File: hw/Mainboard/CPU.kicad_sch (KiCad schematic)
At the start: 10 parts, among them U11 W65C02S, U12 AS6C1008

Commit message: wip: pre-routing
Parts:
- removed JP7: A10 SEL, Jumper:SolderJumper-3_P1.3mm_Open_RoundedPad1.0x1.5mm, symbol Jumper:SolderJumper_3_Open
- removed JP8: A11 SEL, Jumper:SolderJumper-3_P1.3mm_Open_RoundedPad1.0x1.5mm, symbol Jumper:SolderJumper_3_Open
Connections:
- net RAM_A10: now also U12.31 (A15)
- net RAM_A11: now also U12.28 (A13)
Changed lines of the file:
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@@
-    (stroke (width 0) (type default) (color 0 0 0 0))
-  )
-  (bus_entry (at 148.59 43.18) (size -2.54 2.54)
     (stroke (width 0) (type default) (color 0 0 0 0))
   )
@@
     (stroke (width 0) (type default) (color 0 0 0 0))
   )
-  (bus_entry (at 148.59 36.83) (size -2.54 2.54)
-    (stroke (width 0) (type default) (color 0 0 0 0))
-  )
   (bus_entry (at 218.44 67.31) (size 2.54 -2.54)
     (stroke (width 0) (type default) (color 0 0 0 0))
@@
     (stroke (width 0) (type default) (color 0 0 0 0))
   )
-  (wire (pts (xy 167.64 36.83) (xy 218.44 36.83))
+  (wire (pts (xy 162.56 36.83) (xy 218.44 36.83))
     (stroke (width 0) (type default) (color 0 0 0 0))
   )
@@
     (stroke (width 0) (type default) (color 0 0 0 0))
   )
-  (wire (pts (xy 148.59 43.18) (xy 167.64 43.18))
-    (stroke (width 0) (type default) (color 0 0 0 0))
-  )
   (wire (pts (xy 162.56 95.25) (xy 185.42 95.25))
     (stroke (width 0) (type default) (color 0 0 0 0))
@@
     (stroke (width 0) (type default) (color 0 0 0 0))
   )
-  (wire (pts (xy 172.72 46.99) (xy 172.72 90.17))
+  (wire (pts (xy 172.72 43.18) (xy 172.72 90.17))
     (stroke (width 0) (type default) (color 0 0 0 0))
   )
@@
     (stroke (width 0) (type default) (color 0 0 0 0))
   )
-  (bus (pts (xy 146.05 39.37) (xy 146.05 29.21))
-    (stroke (width 0) (type default) (color 0 0 0 0))
-  )
   (bus (pts (xy 124.46 95.25) (xy 124.46 97.79))
     (stroke (width 0) (type default) (color 0 0 0 0))
@@
     (stroke (width 0) (type default) (color 0 0 0 0))
   )
-  (bus (pts (xy 146.05 59.69) (xy 146.05 45.72))
-    (stroke (width 0) (type default) (color 0 0 0 0))
-  )
   (wire (pts (xy 148.59 69.85) (xy 185.42 69.85))
     (stroke (width 0) (type default) (color 0 0 0 0))
@@
     (stroke (width 0) (type default) (color 0 0 0 0))
   )
-  (wire (pts (xy 162.56 95.25) (xy 162.56 40.64))
+  (wire (pts (xy 162.56 36.83) (xy 162.56 95.25))
     (stroke (width 0) (type default) (color 0 0 0 0))
   )
@@
     (stroke (width 0) (type default) (color 0 0 0 0))
   )
-  (bus (pts (xy 146.05 45.72) (xy 146.05 39.37))
+  (bus (pts (xy 146.05 29.21) (xy 146.05 59.69))
     (stroke (width 0) (type default) (color 0 0 0 0))
   )
@@
     (stroke (width 0) (type default) (color 0 0 0 0))
   )
-  (wire (pts (xy 148.59 36.83) (xy 157.48 36.83))
-    (stroke (width 0) (type default) (color 0 0 0 0))
-  )
   (wire (pts (xy 73.66 80.01) (xy 87.63 80.01))
     (stroke (width 0) (type default) (color 0 0 0 0))
@@
     (stroke (width 0) (type default) (color 0 0 0 0))
   )
-  (wire (pts (xy 177.8 43.18) (xy 218.44 43.18))
+  (wire (pts (xy 172.72 43.18) (xy 218.44 43.18))
     (stroke (width 0) (type default) (color 0 0 0 0))
   )
@@
     (effects (font (size 1.27 1.27)) (justify left bottom))
   )
-  (label "A10" (at 148.59 36.83 0)
-    (effects (font (size 1.27 1.27)) (justify left bottom))
-  )
   (label "D5" (at 118.11 113.03 0)
     (effects (font (size 1.27 1.27)) (justify left bottom))
@@
   (label "D6" (at 218.44 59.69 180)
     (effects (font (size 1.27 1.27)) (justify right bottom))
-  )
-  (label "A11" (at 148.59 43.18 0)
-    (effects (font (size 1.27 1.27)) (justify left bottom))
   )
   (label "A2" (at 148.59 87.63 0)
@@
     (pin "2")
   )
-  (symbol (lib_id "Jumper:SolderJumper_3_Open") (at 162.56 36.83 0) (mirror y) (unit 1)
-    (in_bom yes) (on_board yes)
-    (property "Reference" "JP7" (id 0) (at 162.56 31.75 0))
-    (property "Value" "A10 SEL" (id 1) (at 162.56 34.29 0))
-    (property "Footprint" "Jumper:SolderJumper-3_P1.3mm_Open_RoundedPad1.0x1.5mm" (id 2) (at 162.56 36.83 0)
-      (effects (font (size 1.27 1.27)) hide)
-    )
-    (property "Datasheet" "~" (id 3) (at 162.56 36.83 0)
-      (effects (font (size 1.27 1.27)) hide)
-    )
-    (pin "1")
-    (pin "2")
-    (pin "3")
-  )
-  (symbol (lib_id "Jumper:SolderJumper_3_Open") (at 172.72 43.18 0) (mirror y) (unit 1)
-    (in_bom yes) (on_board yes)
-    (property "Reference" "JP8" (id 0) (at 172.72 38.1 0))
-    (property "Value" "A11 SEL" (id 1) (at 172.72 40.64 0))
-    (property "Footprint" "Jumper:SolderJumper-3_P1.3mm_Open_RoundedPad1.0x1.5mm" (id 2) (at 172.72 43.18 0)
-      (effects (font (size 1.27 1.27)) hide)
-    )
-    (property "Datasheet" "~" (id 3) (at 172.72 43.18 0)
-      (effects (font (size 1.27 1.27)) hide)
-    )
-    (pin "1")
-    (pin "2")
-    (pin "3")
-  )
   (symbol (lib_id "power:GND") (at 102.87 124.46 0) (unit 1)

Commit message: Document schematics
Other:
- note added: "To improve routing, A[0..16] and D[0..7] and arbitrarily assigned to the address and data pins of the SRAM. RAM_A[10..11] are used to mirror the screen RAM when the CPU accesses range $8000-8FFF. 40 col PET has 1k of screen RAM, mirrored 4 times. 80 col PET has 2k of screen RAM, mirrored 2 times."
- note removed: "40 col PET has 1k of video RAM, mirrored 4 times. 80 col PET has 2k of video RAM, mirrored 2 times. 111111 addr 5432109876543210 8000: 1000000000000000 8400: 1000010000000000 8800: 1000100000000000 8C00: 1000110000000000"
- note removed: "TODO: Reroute RAM Addr and Data"
- moved on the sheet: C10, C11
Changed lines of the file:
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@@
   (junction (at 68.58 57.15) (diameter 0) (color 0 0 0 0)
   )
-  (junction (at 55.88 156.21) (diameter 0) (color 0 0 0 0)
+  (junction (at 71.12 170.18) (diameter 0) (color 0 0 0 0)
   )
   (junction (at 78.74 77.47) (diameter 0) (color 0 0 0 0)
@@
   (junction (at 68.58 46.99) (diameter 0) (color 0 0 0 0)
   )
-  (junction (at 55.88 148.59) (diameter 0) (color 0 0 0 0)
+  (junction (at 71.12 162.56) (diameter 0) (color 0 0 0 0)
   )
   (no_connect (at 87.63 107.95))
@@
     (stroke (width 0) (type default) (color 0 0 0 0))
   )
-  (wire (pts (xy 55.88 148.59) (xy 66.04 148.59))
+  (wire (pts (xy 71.12 162.56) (xy 81.28 162.56))
     (stroke (width 0) (type default) (color 0 0 0 0))
   )
@@
     (stroke (width 0) (type default) (color 0 0 0 0))
   )
-  (wire (pts (xy 66.04 154.94) (xy 66.04 156.21))
-    (stroke (width 0) (type default) (color 0 0 0 0))
-  )
-  (wire (pts (xy 66.04 156.21) (xy 55.88 156.21))
+  (wire (pts (xy 81.28 168.91) (xy 81.28 170.18))
+    (stroke (width 0) (type default) (color 0 0 0 0))
+  )
+  (wire (pts (xy 81.28 170.18) (xy 71.12 170.18))
     (stroke (width 0) (type default) (color 0 0 0 0))
   )
@@
     (stroke (width 0) (type default) (color 0 0 0 0))
   )
-  (wire (pts (xy 45.72 149.86) (xy 45.72 148.59))
+  (wire (pts (xy 60.96 163.83) (xy 60.96 162.56))
     (stroke (width 0) (type default) (color 0 0 0 0))
   )
@@
     (stroke (width 0) (type default) (color 0 0 0 0))
   )
-  (wire (pts (xy 45.72 156.21) (xy 45.72 154.94))
+  (wire (pts (xy 60.96 170.18) (xy 60.96 168.91))
     (stroke (width 0) (type default) (color 0 0 0 0))
   )
@@
     (stroke (width 0) (type default) (color 0 0 0 0))
   )
-  (wire (pts (xy 55.88 156.21) (xy 45.72 156.21))
+  (wire (pts (xy 71.12 170.18) (xy 60.96 170.18))
     (stroke (width 0) (type default) (color 0 0 0 0))
   )
@@
     (stroke (width 0) (type default) (color 0 0 0 0))
   )
-  (wire (pts (xy 45.72 148.59) (xy 55.88 148.59))
+  (wire (pts (xy 60.96 162.56) (xy 71.12 162.56))
     (stroke (width 0) (type default) (color 0 0 0 0))
   )
@@
     (stroke (width 0) (type default) (color 0 0 0 0))
   )
-  (wire (pts (xy 66.04 148.59) (xy 66.04 149.86))
+  (wire (pts (xy 81.28 162.56) (xy 81.28 163.83))
     (stroke (width 0) (type default) (color 0 0 0 0))
   )
@@
     (stroke (width 0) (type default) (color 0 0 0 0))
   )
-  (text "TODO: Reroute RAM Addr and Data" (at 227.33 104.14 0)
+  (text "To improve routing, A[0..16] and D[0..7] and arbitrarily assigned to\nthe address and data pins of the SRAM.\n\nRAM_A[10..11] are used to mirror the screen RAM when the CPU accesses\nrange $8000-8FFF.\n\n40 col PET has 1k of screen RAM, mirrored 4 times.\n80 col PET has 2k of screen RAM, mirrored 2 times.\n"
+    (at 166.37 148.59 0)
     (effects (font (size 1.27 1.27)) (justify left bottom))
   )
   (text " RAM\n128KB" (at 195.58 86.36 0)
-    (effects (font (size 1.27 1.27)) (justify left bottom))
-  )
-  (text "40 col PET has 1k of video RAM, mirrored 4 times.\n80 col PET has 2k of video RAM, mirrored 2 times.\n\n      111111\naddr  5432109876543210\n8000: 1000000000000000\n8400: 1000010000000000\n8800: 1000100000000000\n8C00: 1000110000000000\n"
-    (at 143.51 160.02 0)
     (effects (font (size 1.27 1.27)) (justify left bottom))
   )
@@
     (pin "2")
   )
-  (symbol (lib_id "Device:C_Small") (at 45.72 152.4 0) (unit 1)
-    (in_bom yes) (on_board yes)
-    (property "Reference" "C10" (id 0) (at 48.0568 151.2316 0)
+  (symbol (lib_id "Device:C_Small") (at 60.96 166.37 0) (unit 1)
+    (in_bom yes) (on_board yes)
+    (property "Reference" "C10" (id 0) (at 63.2968 165.2016 0)
       (effects (font (size 1.27 1.27)) (justify left))
     )
-    (property "Value" "100n" (id 1) (at 48.0568 153.543 0)
+    (property "Value" "100n" (id 1) (at 63.2968 167.513 0)
       (effects (font (size 1.27 1.27)) (justify left))
     )
-    (property "Footprint" "Capacitor_SMD:C_0402_1005Metric" (id 2) (at 45.72 152.4 0)
-      (effects (font (size 1.27 1.27)) hide)
-    )
-    (property "Datasheet" "~" (id 3) (at 45.72 152.4 0)
-      (effects (font (size 1.27 1.27)) hide)
-    )
-    (property "LCSC" "C1525" (id 4) (at 45.72 152.4 0)
+    (property "Footprint" "Capacitor_SMD:C_0402_1005Metric" (id 2) (at 60.96 166.37 0)
+      (effects (font (size 1.27 1.27)) hide)
+    )
+    (property "Datasheet" "~" (id 3) (at 60.96 166.37 0)
+      (effects (font (size 1.27 1.27)) hide)
+    )
+    (property "LCSC" "C1525" (id 4) (at 60.96 166.37 0)
       (effects (font (size 1.27 1.27)) hide)
     )
@@
     (pin "2")
   )
-  (symbol (lib_id "Device:C_Small") (at 66.04 152.4 0) (unit 1)
-    (in_bom yes) (on_board yes)
-    (property "Reference" "C11" (id 0) (at 68.3768 151.2316 0)
+  (symbol (lib_id "Device:C_Small") (at 81.28 166.37 0) (unit 1)
+    (in_bom yes) (on_board yes)
+    (property "Reference" "C11" (id 0) (at 83.6168 165.2016 0)
       (effects (font (size 1.27 1.27)) (justify left))
     )
-    (property "Value" "100n" (id 1) (at 68.3768 153.543 0)
+    (property "Value" "100n" (id 1) (at 83.6168 167.513 0)
       (effects (font (size 1.27 1.27)) (justify left))
     )
-    (property "Footprint" "Capacitor_SMD:C_0402_1005Metric" (id 2) (at 66.04 152.4 0)
-      (effects (font (size 1.27 1.27)) hide)
-    )
-    (property "Datasheet" "~" (id 3) (at 66.04 152.4 0)
-      (effects (font (size 1.27 1.27)) hide)
-    )
-    (property "LCSC" "C1525" (id 4) (at 66.04 152.4 0)
+    (property "Footprint" "Capacitor_SMD:C_0402_1005Metric" (id 2) (at 81.28 166.37 0)
+      (effects (font (size 1.27 1.27)) hide)
+    )
+    (property "Datasheet" "~" (id 3) (at 81.28 166.37 0)
+      (effects (font (size 1.27 1.27)) hide)
+    )
+    (property "LCSC" "C1525" (id 4) (at 81.28 166.37 0)
       (effects (font (size 1.27 1.27)) hide)
     )
@@
     (pin "2")
   )
-  (symbol (lib_id "power:+3V3") (at 55.88 148.59 0) (unit 1)
-    (in_bom yes) (on_board yes)
-    (property "Reference" "#PWR047" (id 0) (at 55.88 152.4 0)
-      (effects (font (size 1.27 1.27)) hide)
-    )
-    (property "Value" "+3V3" (id 1) (at 56.261 144.1958 0))
-    (property "Footprint" "" (id 2) (at 55.88 148.59 0)
-      (effects (font (size 1.27 1.27)) hide)
-    )
-    (property "Datasheet" "" (id 3) (at 55.88 148.59 0)
-      (effects (font (size 1.27 1.27)) hide)
-    )
-    (pin "1")
-  )
-  (symbol (lib_id "power:GND") (at 55.88 156.21 0) (unit 1)
-    (in_bom yes) (on_board yes)
-    (property "Reference" "#PWR048" (id 0) (at 55.88 162.56 0)
-      (effects (font (size 1.27 1.27)) hide)
-    )
-    (property "Value" "GND" (id 1) (at 56.007 160.6042 0))
-    (property "Footprint" "" (id 2) (at 55.88 156.21 0)
-      (effects (font (size 1.27 1.27)) hide)
-    )
-    (property "Datasheet" "" (id 3) (at 55.88 156.21 0)
-      (effects (font (size 1.27 1.27)) hide)
-    )
+  (symbol (lib_id "power:+3V3") (at 71.12 162.56 0) (unit 1)
+    (in_bom yes) (on_board yes)
+    (property "Reference" "#PWR047" (id 0) (at 71.12 166.37 0)
+      (effects (font (size 1.27 1.27)) hide)
+    )
+    (property "Value" "+3V3" (id 1) (at 71.501 158.1658 0))
+    (property "Footprint" "" (id 2) (at 71.12 162.56 0)
+      (effects (font (size 1.27 1.27)) hide)
+    )
+    (property "Datasheet" "" (id 3) (at 71.12 162.56 0)
+      (effects (font (size 1.27 1.27)) hide)
+    )
+    (pin "1")
+  )
+  (symbol (lib_id "power:GND") (at 71.12 170.18 0) (unit 1)
+    (in_bom yes) (on_board yes)
+    (property "Reference" "#PWR048" (id 0) (at 71.12 176.53 0)
+      (effects (font (size 1.27 1.27)) hide)
+    )
+    (property "Value" "GND" (id 1) (at 71.247 174.5742 0))
+    (property "Footprint" "" (id 2) (at 71.12 170.18 0)
+      (effects (font (size 1.27 1.27)) hide)
+    )
+    (property "Datasheet" "" (id 3) (at 71.12 170.18 0)
+      (effects (font (size 1.27 1.27)) hide)
+    )

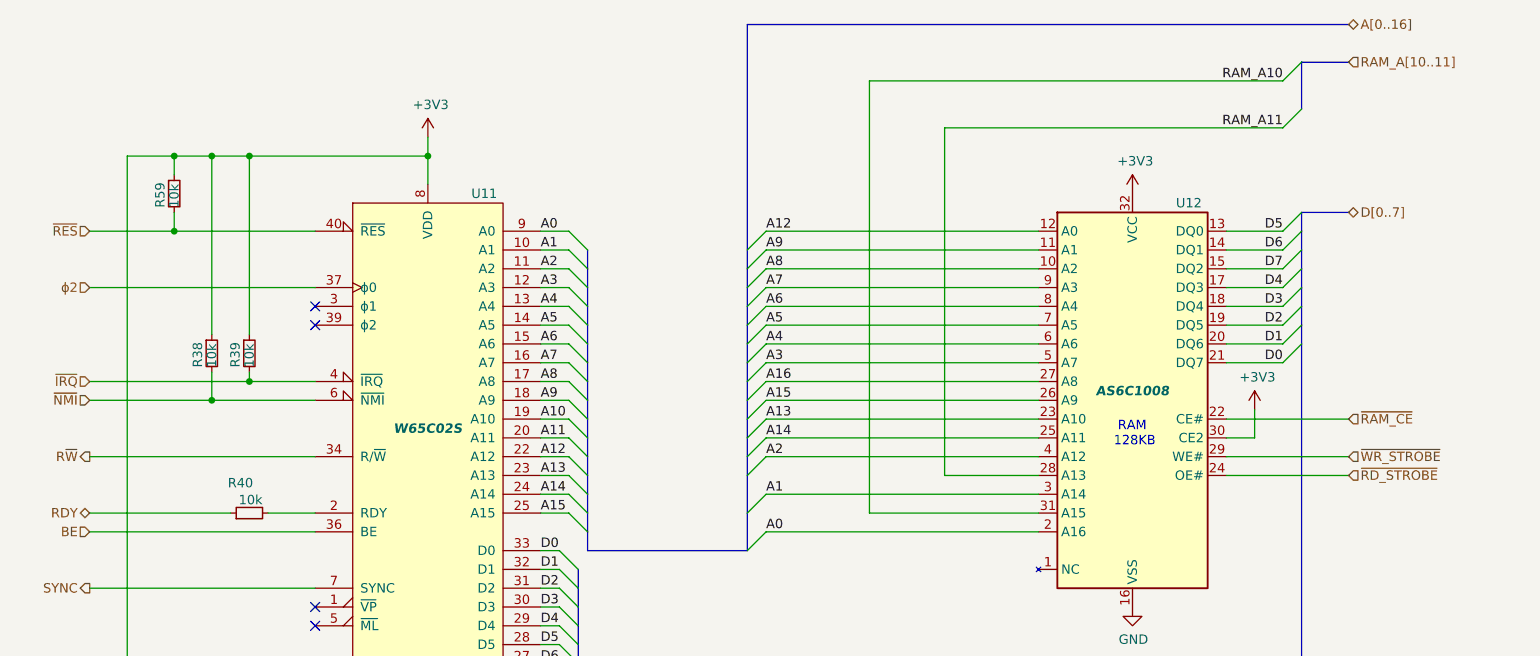
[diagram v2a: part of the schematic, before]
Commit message: hw: more schematic comments / cleanup
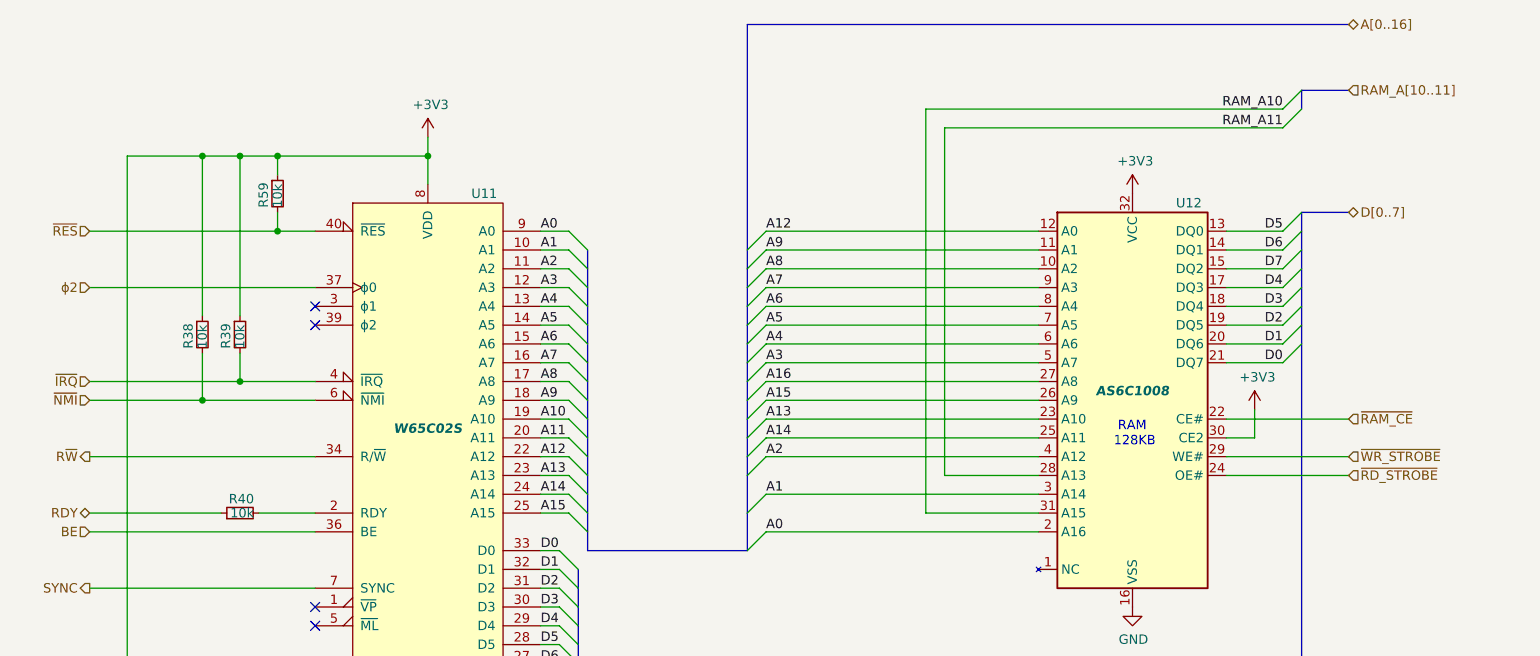
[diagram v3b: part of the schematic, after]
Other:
- moved on the sheet: R38, R39, R40, R59

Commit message: hw: T8 (wip)
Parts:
- added R24: 10k, Resistor_SMD:R_0402_1005Metric, symbol Device:R_Small
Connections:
- net +3V3: now also R24.1; no longer U11.38 (~{SO})
- net A12: now also U12.27 (A8); no longer U12.12 (A0)
- net A13: now also U12.28 (A13); no longer U12.23 (A10)
- net A16: now also U12.31 (A15); no longer U12.27 (A8)
- net D1: now also U12.13 (DQ0); no longer U12.20 (DQ6)
- net D2: now also U12.20 (DQ6); no longer U12.19 (DQ5)
- net D3: now also U12.14 (DQ1); no longer U12.18 (DQ4)
- net D4: now also U12.19 (DQ5); no longer U12.17 (DQ3)
- net D5: now also U12.15 (DQ2); no longer U12.13 (DQ0)
- net D6: now also U12.18 (DQ4); no longer U12.14 (DQ1)
- net D7: now also U12.17 (DQ3); no longer U12.15 (DQ2)
- net RAM_A10: now also U12.12 (A0); no longer U12.31 (A15)
- net RAM_A11: now also U12.23 (A10); no longer U12.28 (A13)
- net ~{VP}: now reaches U11.1 (~{VP})
- net ~{ML}: now reaches U11.5 (~{ML})
- new net ~{SO}: R24.2, U11.38 (~{SO})
- no-connect marks 4 -> 2

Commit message: hw: routing (excluding MCU)
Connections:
- net A12: now also U12.31 (A15); no longer U12.27 (A8)
- net A14: now also U12.27 (A8); no longer U12.25 (A11)
- net A16: now also U12.25 (A11); no longer U12.31 (A15)
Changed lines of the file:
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@@
     (effects (font (size 1.27 1.27)) (justify right bottom))
   )
-  (label "A16" (at 185.42 95.25 180)
+  (label "A16" (at 185.42 85.09 180)
     (effects (font (size 1.27 1.27)) (justify right bottom))
   )
@@
     (effects (font (size 1.27 1.27)) (justify right bottom))
   )
-  (label "A14" (at 185.42 85.09 180)
+  (label "A14" (at 185.42 77.47 180)
     (effects (font (size 1.27 1.27)) (justify right bottom))
   )
@@
     (effects (font (size 1.27 1.27)) (justify left bottom))
   )
-  (label "A12" (at 185.42 77.47 180)
+  (label "A12" (at 185.42 95.25 180)
     (effects (font (size 1.27 1.27)) (justify right bottom))
   )

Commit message: hw: routable (wip)
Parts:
- removed R24: 10k, Resistor_SMD:R_0402_1005Metric, symbol Device:R_Small
- R38, R39, R40, R59: value 10k -> 4k7; LCSC C25744 -> C25900
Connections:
- net +3V3: now also R40.2
- net GND: no longer U11.21 (VSS), U12.16 (VSS)
- net RDY: now also U11.2 (RDY)
- new net PD_GND: U11.21 (VSS), U12.16 (VSS)
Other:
- moved on the sheet: R40
